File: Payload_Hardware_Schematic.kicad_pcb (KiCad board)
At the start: 2 copper layers, 10 parts, among them J1 Micro_SD_Card, J2 Conn_01x06_Pin_5V, J3 Conn_01x06_Pin_3V3, J4 Conn_01x04_Pin, J5 Conn_01x08_Pin, U1 STM32F411 BlackPill, U2 MPM3610, U3 BMP388, U4 LSM9DS1, U5 MPM3610

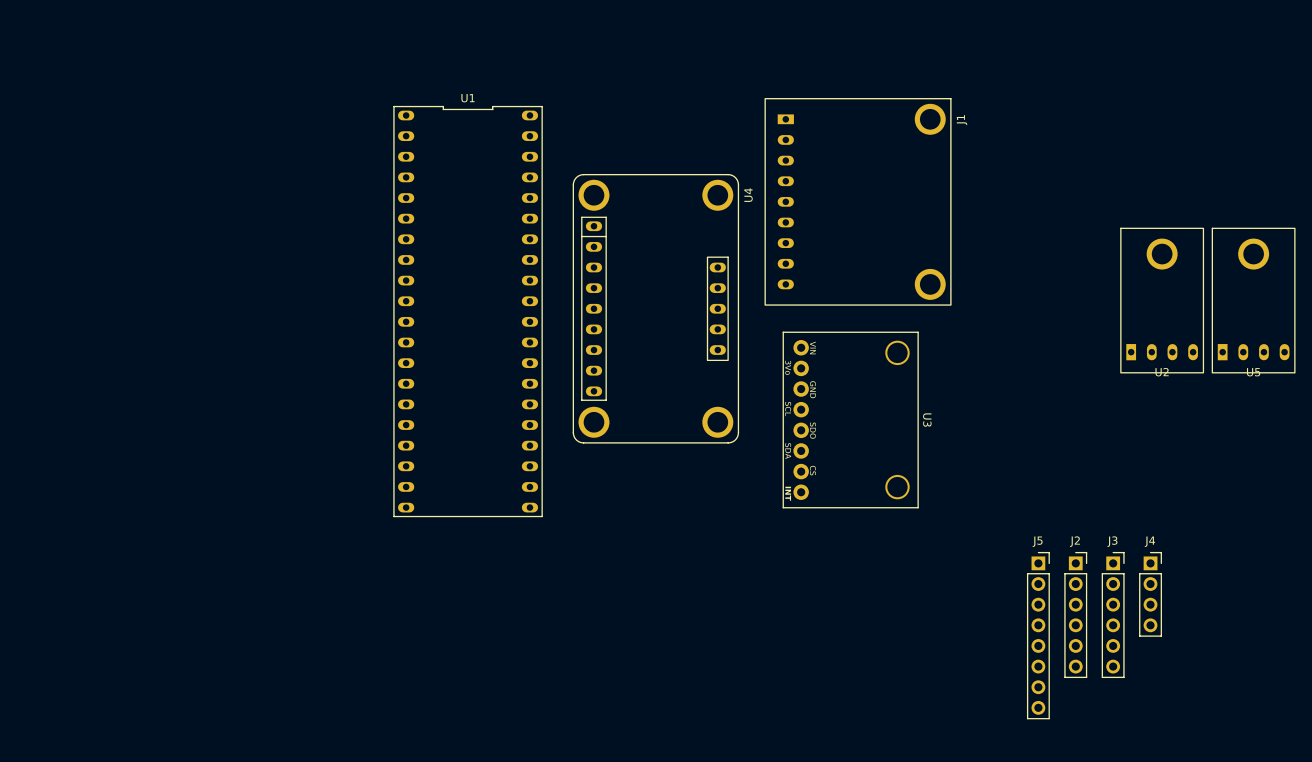
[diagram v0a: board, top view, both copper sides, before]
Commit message: updated footprints
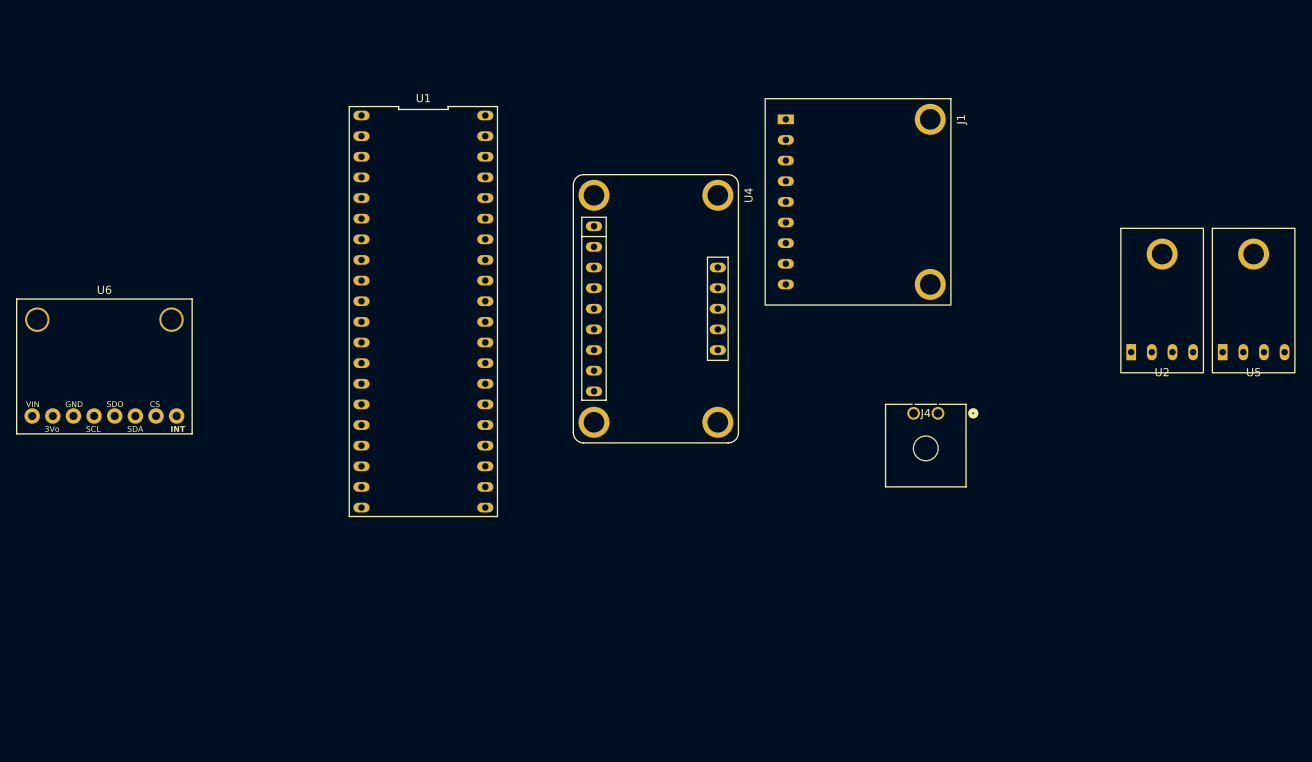
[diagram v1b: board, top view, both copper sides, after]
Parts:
- removed J2: Conn_01x06_Pin_5V, Connector_PinSocket_2.54mm:PinSocket_1x06_P2.54mm_Vertical
- removed J3: Conn_01x06_Pin_3V3, Connector_PinSocket_2.54mm:PinSocket_1x06_P2.54mm_Vertical
- removed J5: Conn_01x08_Pin, Connector_PinSocket_2.54mm:PinSocket_1x08_P2.54mm_Vertical
- removed U3: BMP388, BMP388:BMP388_Breakout
- added U6: BMP388, Payload-BMP388:BMP388_Breakout, F.Cu at (62.2, 59.8)
- J4: value Conn_01x04_Pin -> Conn_01x02; footprint Connector_PinSocket_2.54mm:PinSocket_1x04_P2.54mm_Vertical -> Microfit-Header:CONN_SD-43650-001_02_MOL
- U2, U5: footprint PowerRegulation:MPM3610 -> PowerRugulators:MPM3610
- moved J4 32.0 mm to (164.8, 65.5)
- moved U1 5.50 mm to (101.5, 53.0)
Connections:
- J1 pad 2: /<NO NET> -> GND
- J1 pad 6: unconnected-(J1-DAT3/CS-Pad6) -> /NSS2
- J1 pad 9: (no net) -> unconnected-(J1-DET-Pad9)
- J4 pad 1: +7.2V -> /7.2V
- J4 pad 2: +7.2V -> GND
- U1 pad 19: /GNDSTM -> GND
- U1 pad 21: /VBAT -> GND
- U1 pad 26: /CSMAG -> unconnected-(U1-A0-Pad26)
- U1 pad 28: unconnected-(U1-A2-Pad28) -> /UART_TX
- U1 pad 29: unconnected-(U1-A3-Pad29) -> /UART_RX
- U1 pad 30: /NSS1 -> unconnected-(U1-A4-Pad30)
- U1 pad 31: /SCK1 -> unconnected-(U1-A5-Pad31)
- U1 pad 32: /MISO1 -> unconnected-(U1-A6-Pad32)
- U1 pad 33: /MOSI1 -> unconnected-(U1-A7-Pad33)
- U2 pad 2: Net-(J2-Pin_1) -> /5V
- U2 pad 3: +7.2V -> /7.2V
- U4 pad 1: /VIN4 -> GND
- U4 pad 3: /GND4 -> GND
- U4 pad 7: /CSMAG -> unconnected-(U4-CSM-Pad7)
- U5 pad 2: Net-(J3-Pin_1) -> GND
- U5 pad 3: +7.2V -> /7.2V

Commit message: fixed errors and schematic updates
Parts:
- added J2: Conn_01x02_Socket, Connector_PinSocket_2.54mm:PinSocket_1x02_P2.54mm_Vertical, F.Cu at (98.5, 98.5)
- moved U5 138.1 mm to (66.0, 47.6)
- moved U2 45.4 mm to (147.0, 57.9)
- moved J4 25.5 mm to (146.8, 83.5)
- moved U4 20.8 mm to (111.9, 70.5)
- moved J1 18.8 mm to (127.3, 39.3), turned to 0 degrees
- moved U1 7.38 mm to (94.1, 53.2)
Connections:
- J1 pad 1: GND -> /<NO NET>
- J1 pad 2: GND -> /GND
- J4 pad 2: GND -> /GND
- U1 pad 19: GND -> unconnected-(U1-G-Pad19)
- U1 pad 21: GND -> /<NO NET>
- U1 pad 39: unconnected-(U1-G-Pad39) -> /GND
- U2 pad 1: GND -> /GND
- U4 pad 1: GND -> /<NO NET>
- U4 pad 3: GND -> /GND
- U5 pad 1: GND -> /GND
- U5 pad 2: GND -> /<NO NET>
- U6 pad 1: GND -> /<NO NET>
- U6 pad 3: GND -> /GND

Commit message: PCB routing-1
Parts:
- moved U5 89.8 mm to (153.0, 69.8)
- moved U6 76.5 mm to (133.2, 88.3)
- moved J2 55.7 mm to (68.5, 51.5)
- moved J1 31.6 mm to (133.0, 70.4)
- moved U1 24.7 mm to (81.6, 74.5), turned to 90 degrees
- moved U2 22.1 mm to (165.5, 69.8)
- moved J4 20.7 mm to (167.1, 79.4)
- moved U4 13.8 mm to (98.9, 75.0)
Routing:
- net /<NO NET>: track 0.00 -> 176.9 mm
- net /MOSI2: track 0.00 -> 104.0 mm
- net /MOSI3: track 0.00 -> 87.4 mm
- net /NSS2: track 0.00 -> 82.1 mm
- net /MISO2: track 0.00 -> 81.1 mm
- net /NSS3: track 0.00 -> 78.4 mm
- net /MISO3: track 0.00 -> 71.1 mm
- net /SCK2: track 0.00 -> 69.3 mm
- net /SCK3: track 0.00 -> 63.9 mm
- net /SCK4: track 0.00 -> 39.2 mm
- net /MOSI4: track 0.00 -> 28.8 mm
- net /CSIMU: track 0.00 -> 28.5 mm
- net /7.2V: track 0.00 -> 23.3 mm
- net /GND: track 0.00 -> 20.9 mm
- net /UART_TX: track 0.00 -> 18.9 mm
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- added copper zone on B.Cu, net (none)
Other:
- board outline added: 109 x 54.5 mm
- board text added: "3Vo"
- board text added: "INT"
- board text added: "SCL"
- board text added: "SDA"

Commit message: servo pins
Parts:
- added J3: Conn_01x04_Pin, Connector_PinHeader_2.54mm:PinHeader_1x04_P2.54mm_Vertical, F.Cu at (69.0, 96.6)
- added J5: Conn_01x04_Pin, Connector_PinHeader_2.54mm:PinHeader_1x04_P2.54mm_Vertical, F.Cu at (69.0, 81.3)
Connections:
- U1 pad 11: unconnected-(U1-B3-Pad11) -> /NSS3
- U1 pad 14: unconnected-(U1-B6-Pad14) -> /CSIMU
- U1 pad 22: unconnected-(U1-C13-Pad22) -> /LED
- U1 pad 23: unconnected-(U1-C14-Pad23) -> /RCC_OSC32_IN
- U1 pad 24: unconnected-(U1-C15-Pad24) -> /RCC_OSC32_OUT
- U1 pad 26: unconnected-(U1-A0-Pad26) -> /BTN
- U1 pad 30: unconnected-(U1-A4-Pad30) -> /NSS1
- U1 pad 34: /NSS3 -> /FDBK1
- U1 pad 35: /CSIMU -> /FDBK2
- U1 pad 5: unconnected-(U1-A8-Pad5) -> /TIM1
- U1 pad 6: unconnected-(U1-A9-Pad6) -> /TIM2

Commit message: PCB Layout 2
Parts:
- removed J2: Conn_01x02_Socket, Connector_PinSocket_2.54mm:PinSocket_1x02_P2.54mm_Vertical
- added J6: Conn_01x04_Socket, Connector_PinSocket_2.54mm:PinSocket_1x04_P2.54mm_Horizontal, F.Cu at (92.8, 56.4)
- J3, J5: footprint Connector_PinHeader_2.54mm:PinHeader_1x04_P2.54mm_Vertical -> Connector_PinHeader_2.54mm:PinHeader_1x04_P2.54mm_Horizontal
- U1: footprint Avionics_Symbols:STM32F411 -> Payload-STM32:STM32F411_Black_Pill
- moved J3 105.1 mm to (167.6, 60.2), turned to 0 degrees
- moved J5 98.5 mm to (167.5, 78.4), turned to 0 degrees
- moved U4 44.6 mm to (143.5, 73.9), turned to 180 degrees
- moved J1 36.8 mm to (96.9, 77.5), turned to 90 degrees
- moved U6 33.1 mm to (134.7, 55.2), turned to -90 degrees
- moved J4 31.8 mm to (169.0, 47.7), turned to 90 degrees
- moved U1 31.1 mm to (112.4, 69.6), turned to 180 degrees
- moved U2 20.8 mm to (161.3, 49.5), turned to 90 degrees
- moved U5 11.1 mm to (161.3, 62.5), turned to 90 degrees
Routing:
- net /<NO NET>: track 176.9 -> 0.00 mm
- net /MOSI2: track 104.0 -> 0.00 mm
- net /MOSI3: track 87.4 -> 0.00 mm
- net /NSS2: track 82.1 -> 0.00 mm
- net /MISO2: track 81.1 -> 0.00 mm
- net /NSS3: track 78.4 -> 0.00 mm
- net /MISO3: track 71.1 -> 0.00 mm
- net /SCK2: track 69.3 -> 0.00 mm
- net /SCK3: track 63.9 -> 0.00 mm
- net /SCK4: track 39.2 -> 0.00 mm
- net /MOSI4: track 28.8 -> 0.00 mm
- net /CSIMU: track 28.5 -> 0.00 mm
- net /7.2V: track 23.3 -> 0.00 mm
- net /GND: track 20.9 -> 0.00 mm
- net /UART_TX: track 18.9 -> 0.00 mm
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- removed copper zone on B.Cu, net (none)
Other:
- board outline removed
- board text removed: "3Vo"
- board text removed: "INT"
- board text removed: "SCL"
- board text removed: "SDA"

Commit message: auto wiring
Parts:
- added H1: MountingHole, MountingHole:MountingHole_3.2mm_M3_DIN965_Pad, F.Cu at (72.0, 44.0)
- added H2: MountingHole, MountingHole:MountingHole_3.2mm_M3_DIN965_Pad, F.Cu at (72.0, 93.0)
- added H3: MountingHole, MountingHole:MountingHole_3.2mm_M3_DIN965_Pad, F.Cu at (183.0, 44.0)
- added H4: MountingHole, MountingHole:MountingHole_3.2mm_M3_DIN965_Pad, F.Cu at (183.0, 93.0)
- J3, J5: footprint Connector_PinHeader_2.54mm:PinHeader_1x04_P2.54mm_Horizontal -> Connector_PinHeader_2.54mm:PinHeader_1x04_P2.54mm_Vertical
- J6: footprint Connector_PinSocket_2.54mm:PinSocket_1x04_P2.54mm_Horizontal -> Connector_PinHeader_2.54mm:PinHeader_1x04_P2.54mm_Horizontal
- moved J6 5.90 mm to (93.0, 50.5)
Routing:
- net /<NO NET>: track 0.00 -> 133.0 mm, vias 0 -> 1
- net /FDBK1: track 0.00 -> 106.5 mm, vias 0 -> 1
- net /MOSI4: track 0.00 -> 101.5 mm
- net /FDBK2: track 0.00 -> 63.8 mm
- net /TIM1: track 0.00 -> 61.6 mm, vias 0 -> 1
- net /TIM2: track 0.00 -> 47.5 mm
- net /SCK3: track 0.00 -> 46.0 mm
- net /CSIMU: track 0.00 -> 39.2 mm
- net /SCK4: track 0.00 -> 37.4 mm, vias 0 -> 1
- net /5V: track 0.00 -> 36.4 mm
- net /MISO2: track 0.00 -> 31.0 mm
- net /MOSI2: track 0.00 -> 27.3 mm
- net /DIO: track 0.00 -> 27.2 mm
- net /SCK: track 0.00 -> 26.2 mm
- net /7.2V: track 0.00 -> 24.1 mm
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- added copper zone on F.Cu, net /GND
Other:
- board outline added: 118 x 56 mm

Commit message: updates
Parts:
- J3, J5: footprint Connector_PinHeader_2.54mm:PinHeader_1x04_P2.54mm_Vertical -> Connector_PinHeader_2.54mm:PinHeader_1x04_P2.54mm_Horizontal
- moved J6 10.3 mm to (85.4, 57.5), turned to 90 degrees
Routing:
- net /MOSI4: track 101.5 -> 45.0 mm
- net /FDBK1: track 106.5 -> 79.8 mm
- net /CSIMU: track 39.2 -> 30.9 mm, vias 0 -> 1
- net /<NO NET>: track 133.0 -> 124.8 mm
- net /MISO2: track 31.0 -> 26.7 mm
- net /SCK: track 26.2 -> 22.4 mm, vias 0 -> 1
- net /UART_TX: track 18.2 -> 21.9 mm
- net /MOSI3: track 10.4 -> 13.8 mm
- net /UART_RX: track 21.4 -> 23.6 mm
- net /SCK3: track 46.0 -> 44.5 mm
- net /5V: track 36.4 -> 37.4 mm
- net /MOSI2: track 27.3 -> 26.7 mm
- net /DIO: track 27.2 -> 26.6 mm
- net /7.2V: track 24.1 -> 23.5 mm

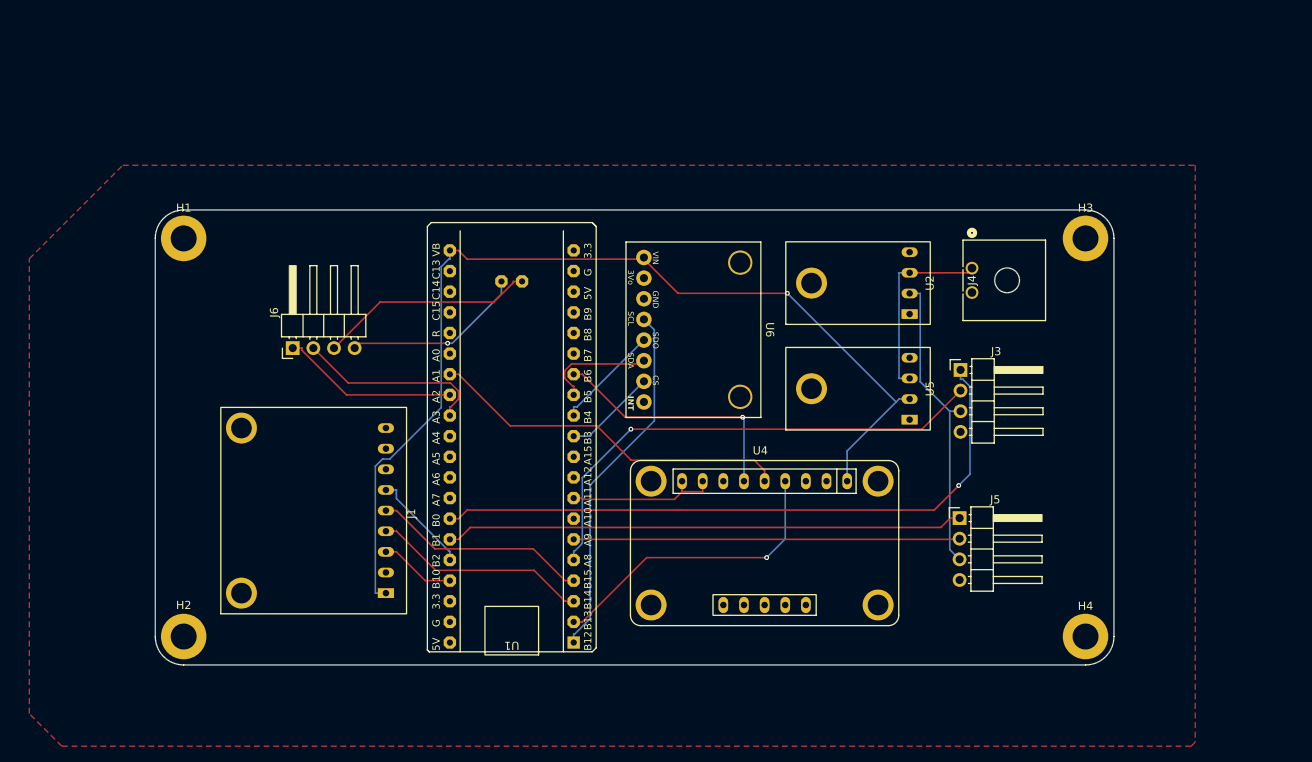
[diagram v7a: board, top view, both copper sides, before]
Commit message: Switched sd card and uart/serial access
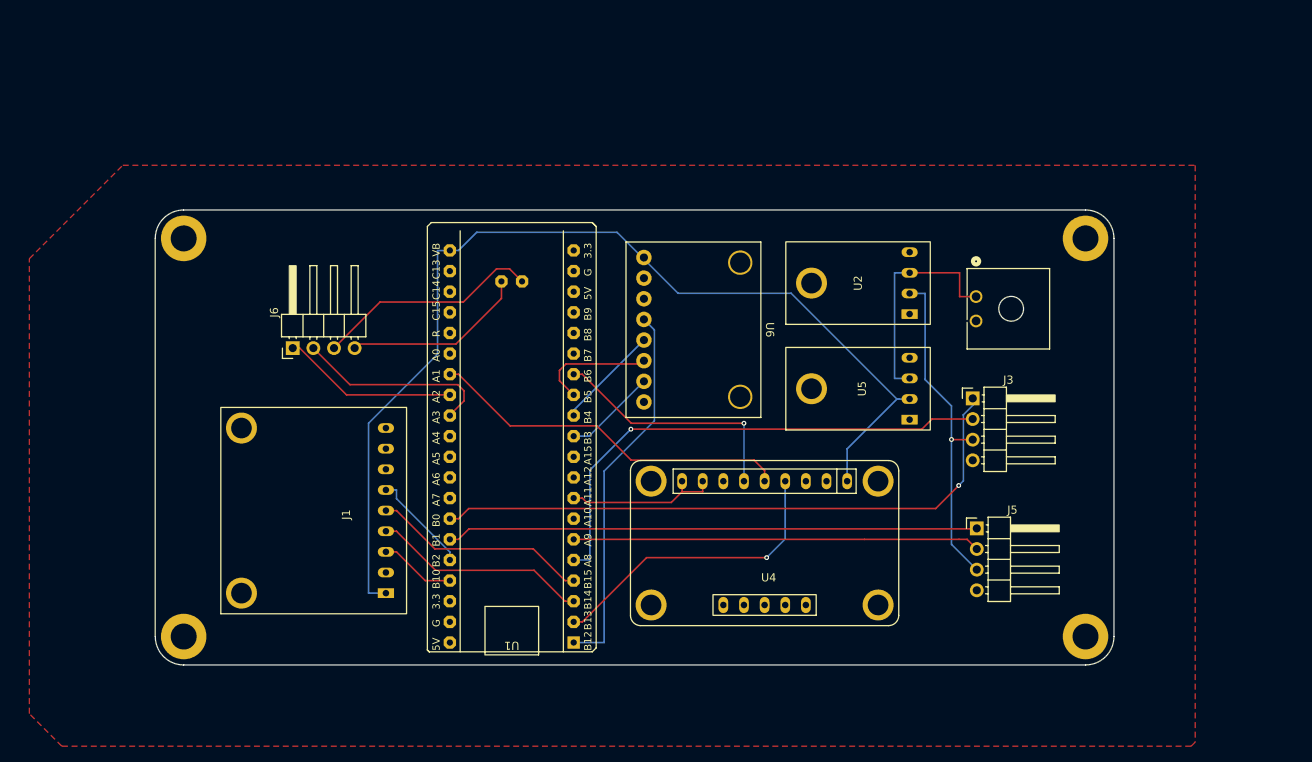
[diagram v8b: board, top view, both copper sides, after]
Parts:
- moved J3 3.81 mm to (169.1, 63.7)
- moved J4 3.54 mm to (169.5, 51.2)
- moved J5 2.47 mm to (169.6, 79.7)
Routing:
- net /7.2V: track 23.5 -> 27.8 mm
- net /FDBK1: track 79.8 -> 75.8 mm
- net /5V: track 37.4 -> 41.2 mm, vias 0 -> 1
- net /<NO NET>: track 124.8 -> 128.2 mm, vias 1 -> 0
- net /TIM2: track 47.5 -> 50.1 mm
- net /SCK3: track 44.5 -> 46.6 mm
- net /FDBK2: track 63.8 -> 65.4 mm
- net /DIO: track 26.6 -> 27.8 mm
- net /TIM1: track 61.6 -> 62.8 mm
- net /UART_RX: track 23.6 -> 24.5 mm
- net /MOSI3: track 13.8 -> 14.6 mm
- net /SCK: track 22.4 -> 22.7 mm, vias 1 -> 0
